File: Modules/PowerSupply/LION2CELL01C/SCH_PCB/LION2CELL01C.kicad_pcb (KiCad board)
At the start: 2 copper layers, 80.8 x 60.5 mm, 98 parts, among them J1 JUMP_4X2, J10 JUMP_2x1, J11 JUMP_2x1, J12 JUMP_2x1, J13 JUMP_4X2, J14 JUMP_2x1, J2 JUMP_2x1, J3 JUMP_2x1, J4 JUMP_2x1, J5 JUMP_2x1, J6 JUMP_2x1, J7 JUMP_4X2, J8 CONN1_1, J9 CONN1_1, P1 _, P2 _, P3 _, P4 _, Q1 IRLML6244, Q2 MMBF170LT1G, Q3 MMBF170LT1G, Q4 BSS83P, SW1 SW_PUSH, U1 BQ29209, U2 BQ24103, U3 BQ34Z100, U4 SN74HC164D

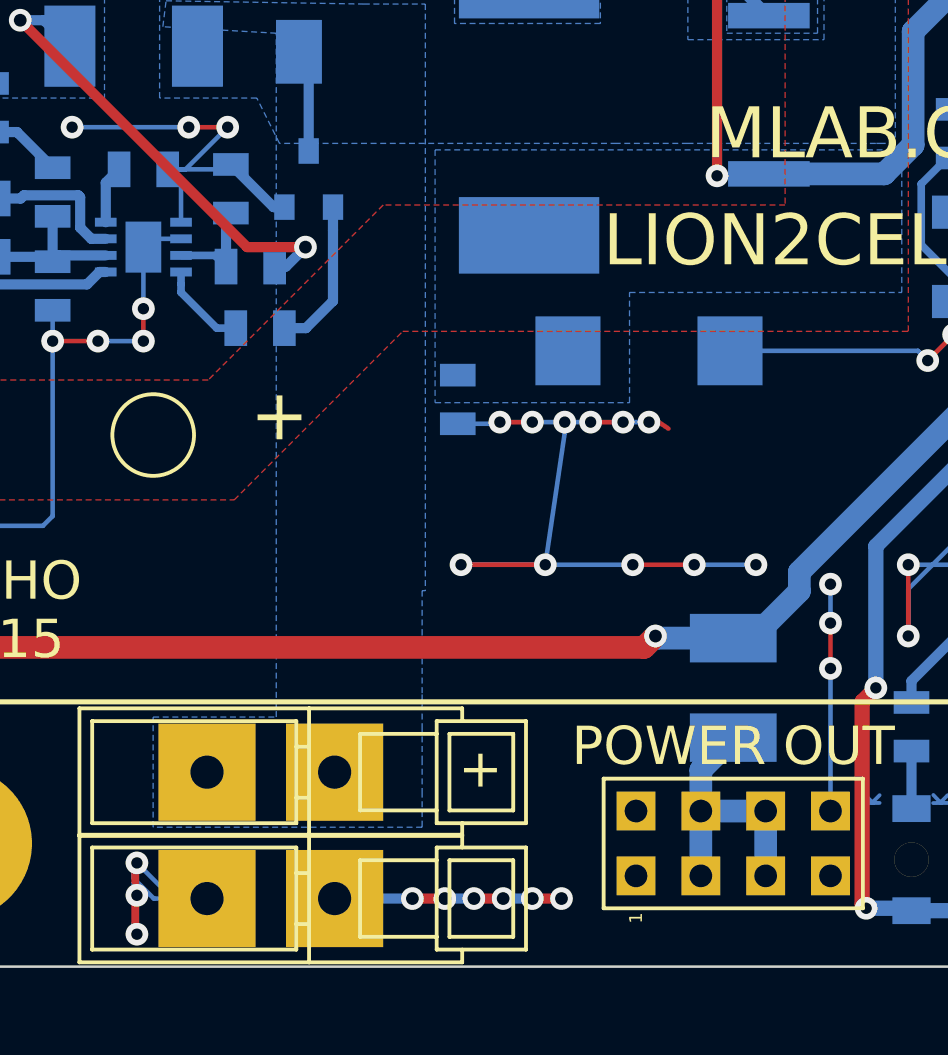
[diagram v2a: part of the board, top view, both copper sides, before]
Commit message: 
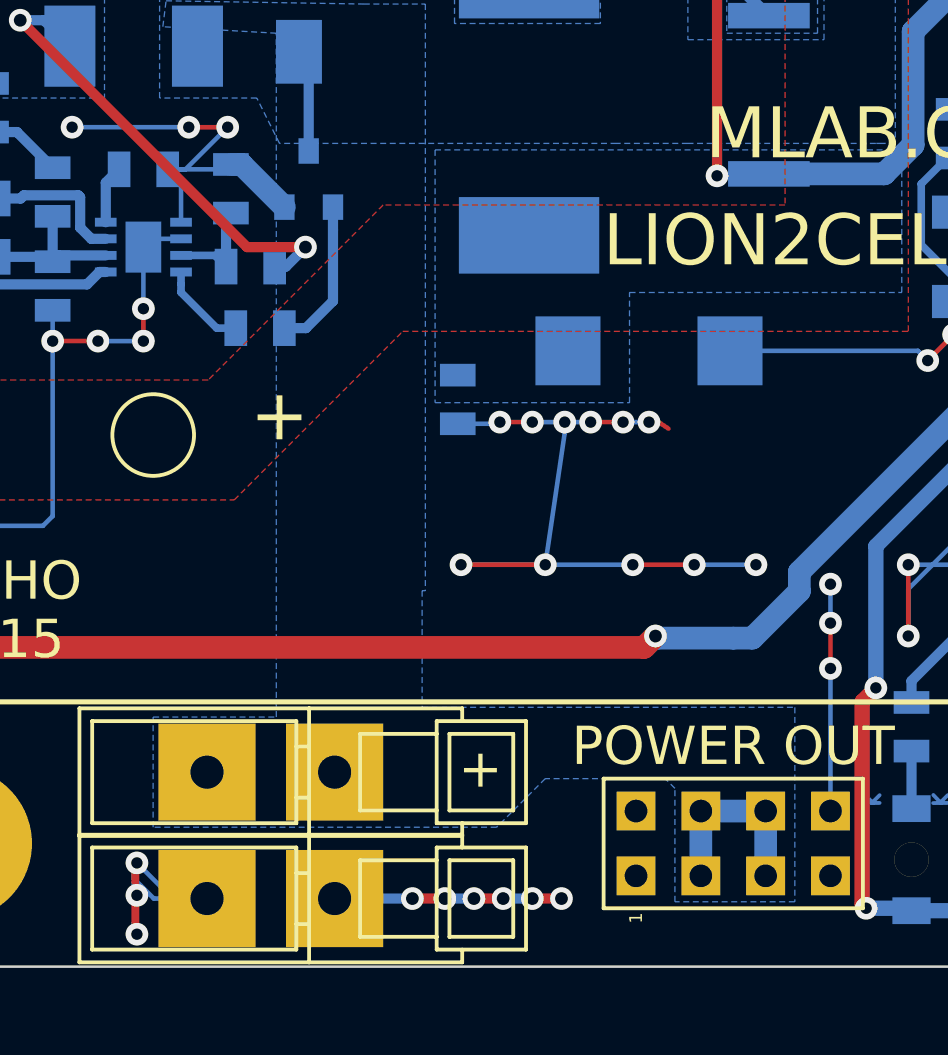
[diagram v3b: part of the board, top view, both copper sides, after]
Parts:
- removed F2: 1,1A, Mlab_F:1812
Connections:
- J7 pad 3: Net-(F2-Pad1) -> /BATTERY+
- J7 pad 4: Net-(F2-Pad1) -> /BATTERY+
- J7 pad 5: Net-(F2-Pad1) -> /BATTERY+
- J7 pad 6: Net-(F2-Pad1) -> /BATTERY+
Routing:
- net Net-(F2-Pad1): track 11.0 -> 0.00 mm
- net /BATTERY+: track 4.04 -> 11.7 mm
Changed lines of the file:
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@@
-(kicad_pcb (version 4) (host pcbnew "(2015-05-13 BZR 5653)-product")
+(kicad_pcb (version 4) (host pcbnew 4.0.0-rc1-stable)
   (general
-    (links 210)
+    (links 209)
     (no_connects 0)
     (area 0.203999 -60.756001 81.076001 -0.203999)
     (thickness 1.6)
     (drawings 31)
-    (tracks 821)
+    (tracks 819)
     (zones 0)
-    (modules 98)
-    (nets 64)
+    (modules 97)
+    (nets 63)
   )
   (page A4)
@@
   )
   (setup
-    (last_trace_width 0.18)
+    (last_trace_width 0.89)
     (user_trace_width 0.2)
     (user_trace_width 0.25)
@@
   (net 60 "Net-(D14-Pad2)")
   (net 61 "Net-(R34-Pad2)")
-  (net 62 "Net-(F2-Pad1)")
-  (net 63 "Net-(F3-Pad1)")
+  (net 62 "Net-(F3-Pad1)")
   (net_class Default "Toto je výchozí třída sítě."
     (clearance 0.18)
@@
     (add_net "Net-(D8-Pad2)")
     (add_net "Net-(D9-Pad2)")
-    (add_net "Net-(F2-Pad1)")
     (add_net "Net-(F3-Pad1)")
     (add_net "Net-(L1-Pad1)")
@@
       (net 3 GND))
     (pad 3 thru_hole rect (at -1.27 -1.27 90) (size 1.524 1.524) (drill 0.889) (layers *.Cu *.Mask F.SilkS)
-      (net 62 "Net-(F2-Pad1)"))
+      (net 56 /BATTERY+))
     (pad 4 thru_hole rect (at 1.27 -1.27 90) (size 1.524 1.524) (drill 0.889) (layers *.Cu *.Mask F.SilkS)
-      (net 62 "Net-(F2-Pad1)"))
+      (net 56 /BATTERY+))
     (pad 5 thru_hole rect (at -1.27 1.27 90) (size 1.524 1.524) (drill 0.889) (layers *.Cu *.Mask F.SilkS)
-      (net 62 "Net-(F2-Pad1)"))
+      (net 56 /BATTERY+))
     (pad 6 thru_hole rect (at 1.27 1.27 90) (size 1.524 1.524) (drill 0.889) (layers *.Cu *.Mask F.SilkS)
-      (net 62 "Net-(F2-Pad1)"))
+      (net 56 /BATTERY+))
     (pad 7 thru_hole rect (at -1.27 3.81 90) (size 1.524 1.524) (drill 0.889) (layers *.Cu *.Mask F.SilkS)
       (net 3 GND))
@@
     (fp_line (start -2.6 1.825) (end 2.6 1.825) (layer B.SilkS) (width 0.15))
     (pad 1 smd rect (at -3.1 0 270) (size 1 3.2) (layers B.Cu B.Paste B.Mask)
-      (net 63 "Net-(F3-Pad1)"))
+      (net 62 "Net-(F3-Pad1)"))
     (pad 2 smd rect (at 3.1 0 270) (size 1 3.2) (layers B.Cu B.Paste B.Mask)
       (net 10 "Net-(C10-Pad1)"))
@@
       (net 31 /CELLS))
     (pad 14 smd rect (at 0.75 1.725 90) (size 0.28 0.85) (layers B.Cu B.Paste B.Mask)
-      (net 63 "Net-(F3-Pad1)"))
+      (net 62 "Net-(F3-Pad1)"))
     (pad 15 smd rect (at 0.25 1.725 90) (size 0.28 0.85) (layers B.Cu B.Paste B.Mask)
       (net 10 "Net-(C10-Pad1)"))
@@
     )
   )
-  (module Mlab_F:1812 (layer B.Cu)
-    (at 35.56 -11.176 90)
-    (descr "Diode Mini-MELF Standard")
-    (tags "Diode Mini-MELF Standard")
-    (attr smd)
-    (fp_text reference F2 (at 0.13462 3.15468 90) (layer B.SilkS)
-      (effects (font (thickness 0.3048)) (justify mirror))
-    )
-    (fp_text value 1,1A (at 0 -3.81 90) (layer B.SilkS) hide
-      (effects (font (thickness 0.3048)) (justify mirror))
-    )
-    (fp_line (start -1.143 -1.778) (end 1.143 -1.778) (layer B.SilkS) (width 0.15))
-    (fp_line (start -1.143 1.778) (end 1.143 1.778) (layer B.SilkS) (width 0.15))
-    (pad 1 smd rect (at -1.95 0 90) (size 1.9 3.4) (layers B.Cu B.Paste B.Mask)
-      (net 62 "Net-(F2-Pad1)"))
-    (pad 2 smd rect (at 1.95 0 90) (size 1.9 3.4) (layers B.Cu B.Paste B.Mask)
-      (net 1 /BAT+))
-    (model MLAB_3D/Diodes/MiniMELF_DO213AA.wrl
-      (at (xyz 0 0 0))
-      (scale (xyz 0.3937 0.3937 0.3937))
-      (rotate (xyz 0 0 0))
-    )
-  )
   (module Mlab_F:2410 (layer B.Cu)
     (at 40.386 -40.894)
@@
     (fp_line (start -1.143 1.778) (end 1.143 1.778) (layer B.SilkS) (width 0.15))
     (pad 1 smd rect (at -2.5 0) (size 2 3.18) (layers B.Cu B.Paste B.Mask)
-      (net 63 "Net-(F3-Pad1)"))
+      (net 62 "Net-(F3-Pad1)"))
     (pad 2 smd rect (at 2.5 0) (size 2 3.18) (layers B.Cu B.Paste B.Mask)
       (net 56 /BATTERY+))
@@
   (segment (start 6.7945 -28.067) (end 8.6995 -28.067) (width 0.4) (layer B.Cu) (net 2))
   (segment (start 8.89 -27.8765) (end 8.89 -29.6545) (width 0.4) (layer B.Cu) (net 2))
+  (segment (start 17.9705 -30.01518) (end 16.29918 -31.6865) (width 0.89) (layer B.Cu) (net 3))
+  (segment (start 16.29918 -31.6865) (end 15.875 -31.6865) (width 0.89) (layer B.Cu) (net 3))
   (segment (start 59.719 -26.842) (end 59.719 -27.247) (width 0.18) (layer B.Cu) (net 3))
   (segment (start 79.502 -36.068) (end 79.502 -28.194) (width 0.18) (layer B.Cu) (net 3))
@@
   (segment (start 72.39 -17.526) (end 73.406 -16.51) (width 0.4) (layer F.Cu) (net 3))
   (segment (start 72.136 -17.526) (end 72.39 -17.526) (width 0.4) (layer F.Cu) (net 3))
-  (segment (start 17.54632 -30.01518) (end 15.875 -31.6865) (width 0.4) (layer B.Cu) (net 3))
-  (segment (start 17.9705 -30.01518) (end 17.54632 -30.01518) (width 0.4) (layer B.Cu) (net 3))
   (segment (start 43.942 -31.9405) (end 42.926 -30.9245) (width 0.3) (layer B.Cu) (net 3))
   (segment (start 44.196 -31.9405) (end 43.942 -31.9405) (width 0.3) (layer B.Cu) (net 3))
@@
   (segment (start 18.923 -32.21482) (end 18.923 -35.72002) (width 0.4) (layer B.Cu) (net 56))
   (segment (start 18.923 -35.72002) (end 18.542 -36.10102) (width 0.4) (layer B.Cu) (net 56))
+  (segment (start 34.29 -3.81) (end 34.29 -6.35) (width 0.89) (layer B.Cu) (net 56))
+  (segment (start 36.83 -6.35) (end 36.83 -3.81) (width 0.89) (layer B.Cu) (net 56))
+  (segment (start 34.29 -6.35) (end 36.83 -6.35) (width 0.89) (layer B.Cu) (net 56))
   (segment (start 62.865 -53.194) (end 62.865 -54.356) (width 0.4) (layer B.Cu) (net 57))
   (segment (start 58.394482 -22.942) (end 57.453979 -23.882503) (width 0.4) (layer B.Cu) (net 57))
@@
   (segment (start 58.439 -14.224) (end 61.214 -11.449) (width 0.4) (layer B.Cu) (net 61))
   (segment (start 61.214 -11.449) (end 61.214 -10.6045) (width 0.4) (layer B.Cu) (net 61))
-  (segment (start 34.29 -3.81) (end 34.29 -6.35) (width 0.89) (layer B.Cu) (net 62))
-  (segment (start 36.83 -6.35) (end 36.83 -3.81) (width 0.89) (layer B.Cu) (net 62))
-  (segment (start 34.29 -6.35) (end 36.83 -6.35) (width 0.89) (layer B.Cu) (net 62))
-  (segment (start 34.29 -7.956) (end 35.56 -9.226) (width 0.89) (layer B.Cu) (net 62))
-  (segment (start 34.29 -6.35) (end 34.29 -7.956) (width 0.89) (layer B.Cu) (net 62))
-  (segment (start 36.058546 -38.608) (end 36.058546 -38.415454) (width 0.4) (layer B.Cu) (net 63))
-  (segment (start 36.058546 -38.415454) (end 36.957 -37.517) (width 0.4) (layer B.Cu) (net 63))
-  (segment (start 36.058546 -38.344546) (end 36.886092 -37.517) (width 0.4) (layer B.Cu) (net 63))
-  (segment (start 36.886092 -37.517) (end 36.957 -37.517) (width 0.4) (layer B.Cu) (net 63))
-  (segment (start 36.058546 -39.315454) (end 33.254539 -42.119461) (width 0.4) (layer B.Cu) (net 63))
-  (segment (start 36.058546 -39.315454) (end 36.058546 -38.608) (width 0.4) (layer B.Cu) (net 63))
-  (segment (start 36.058546 -38.608) (end 36.058546 -38.344546) (width 0.4) (layer B.Cu) (net 63))
-  (segment (start 33.254539 -42.119461) (end 31.036 -44.338) (width 0.4) (layer B.Cu) (net 63))
-  (segment (start 29.223 -44.413) (end 29.400875 -44.413) (width 0.25) (layer B.Cu) (net 63))
-  (segment (start 29.198 -44.438) (end 29.223 -44.413) (width 0.25) (layer B.Cu) (net 63))
-  (segment (start 28.776 -44.438) (end 29.198 -44.438) (width 0.25) (layer B.Cu) (net 63))
-  (segment (start 29.400875 -44.413) (end 30.988 -44.413) (width 0.25) (layer B.Cu) (net 63))
-  (segment (start 31.036 -44.338) (end 30.988 -44.338) (width 0.4) (layer B.Cu) (net 63))
+  (segment (start 36.058546 -38.608) (end 36.058546 -38.415454) (width 0.4) (layer B.Cu) (net 62))
+  (segment (start 36.058546 -38.415454) (end 36.957 -37.517) (width 0.4) (layer B.Cu) (net 62))
+  (segment (start 36.058546 -38.344546) (end 36.886092 -37.517) (width 0.4) (layer B.Cu) (net 62))
+  (segment (start 36.886092 -37.517) (end 36.957 -37.517) (width 0.4) (layer B.Cu) (net 62))
+  (segment (start 36.058546 -39.315454) (end 33.254539 -42.119461) (width 0.4) (layer B.Cu) (net 62))
+  (segment (start 36.058546 -39.315454) (end 36.058546 -38.608) (width 0.4) (layer B.Cu) (net 62))
+  (segment (start 36.058546 -38.608) (end 36.058546 -38.344546) (width 0.4) (layer B.Cu) (net 62))
+  (segment (start 33.254539 -42.119461) (end 31.036 -44.338) (width 0.4) (layer B.Cu) (net 62))
+  (segment (start 29.223 -44.413) (end 29.400875 -44.413) (width 0.25) (layer B.Cu) (net 62))
+  (segment (start 29.198 -44.438) (end 29.223 -44.413) (width 0.25) (layer B.Cu) (net 62))
+  (segment (start 28.776 -44.438) (end 29.198 -44.438) (width 0.25) (layer B.Cu) (net 62))
+  (segment (start 29.400875 -44.413) (end 30.988 -44.413) (width 0.25) (layer B.Cu) (net 62))
+  (segment (start 31.036 -44.338) (end 30.988 -44.338) (width 0.4) (layer B.Cu) (net 62))
   (zone (net 4) (net_name "Net-(C2-Pad1)") (layer B.Cu) (hatch edge 0.508)
     (priority 1)
@@
     (polygon
       (pts
-        (xy 23.368 -10.922) (xy 23.368 -9.652) (xy 23.368 -8.382) (xy 23.368 -7.112) (xy 23.368 -6.35)
-        (xy 23.368 -5.842) (xy 23.368 -5.715) (xy 12.827 -5.715) (xy 12.827 -10.033) (xy 17.653 -10.033)
-        (xy 17.653 -36.83) (xy 13.208 -37.084) (xy 13.335 -38.1) (xy 21.082 -37.973) (xy 23.495 -37.973)
-        (xy 23.495 -14.986) (xy 23.368 -14.986) (xy 23.368 -13.462)
+        (xy 21.082 -37.973) (xy 23.495 -37.973) (xy 23.495 -14.986) (xy 23.368 -14.986) (xy 23.368 -10.414)
+        (xy 37.973 -10.414) (xy 37.973 -2.794) (xy 33.274 -2.794) (xy 33.274 -7.239) (xy 32.893 -7.62)
+        (xy 28.194 -7.62) (xy 26.289 -5.715) (xy 12.827 -5.715) (xy 12.827 -10.033) (xy 17.653 -10.033)
+        (xy 17.653 -36.83) (xy 13.208 -37.084) (xy 13.335 -38.1) (xy 21.082 -37.973)
       )
     )
@@
     )
   )
-  (zone (net 63) (net_name "Net-(F3-Pad1)") (layer B.Cu) (hatch edge 0.508)
+  (zone (net 62) (net_name "Net-(F3-Pad1)") (layer B.Cu) (hatch edge 0.508)
     (priority 1)
     (connect_pads yes (clearance 0.508))

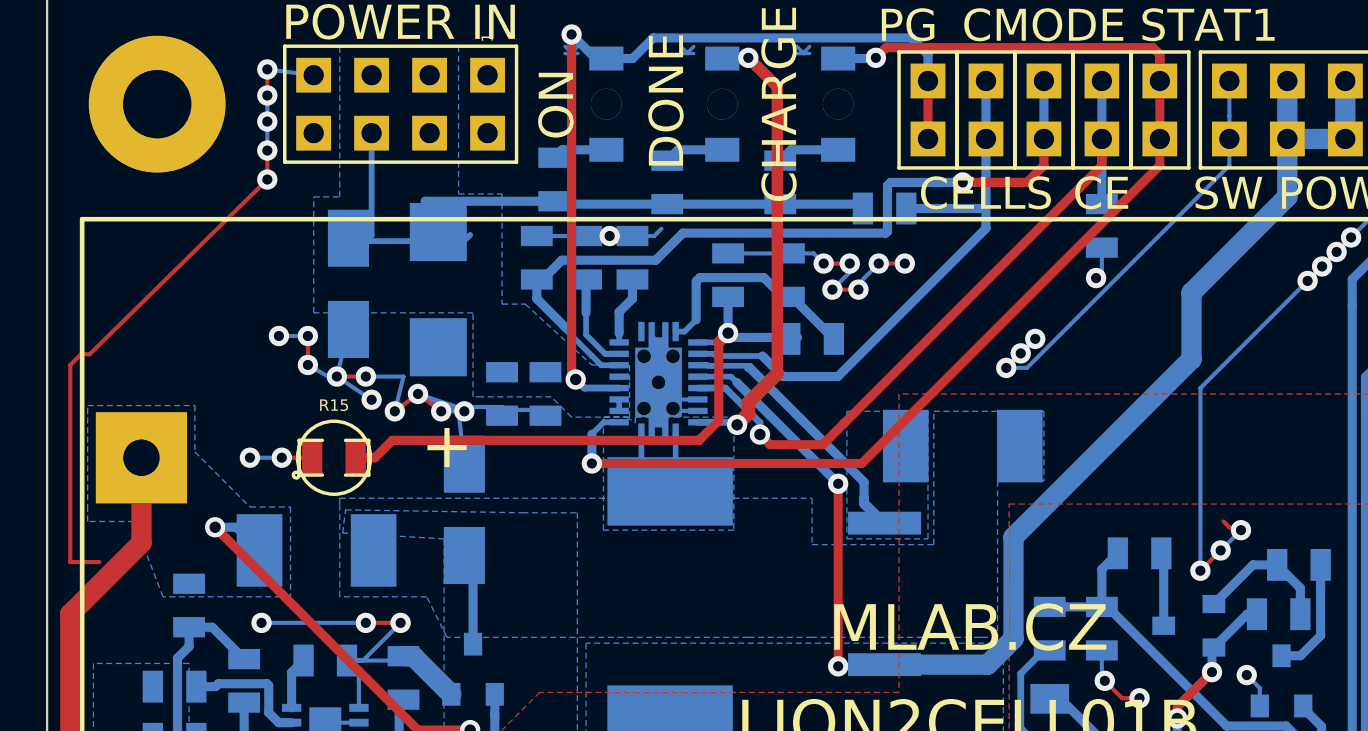
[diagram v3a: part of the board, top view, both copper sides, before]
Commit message: Uprava LION2CELL01C. Generovani vyrobnich dat.
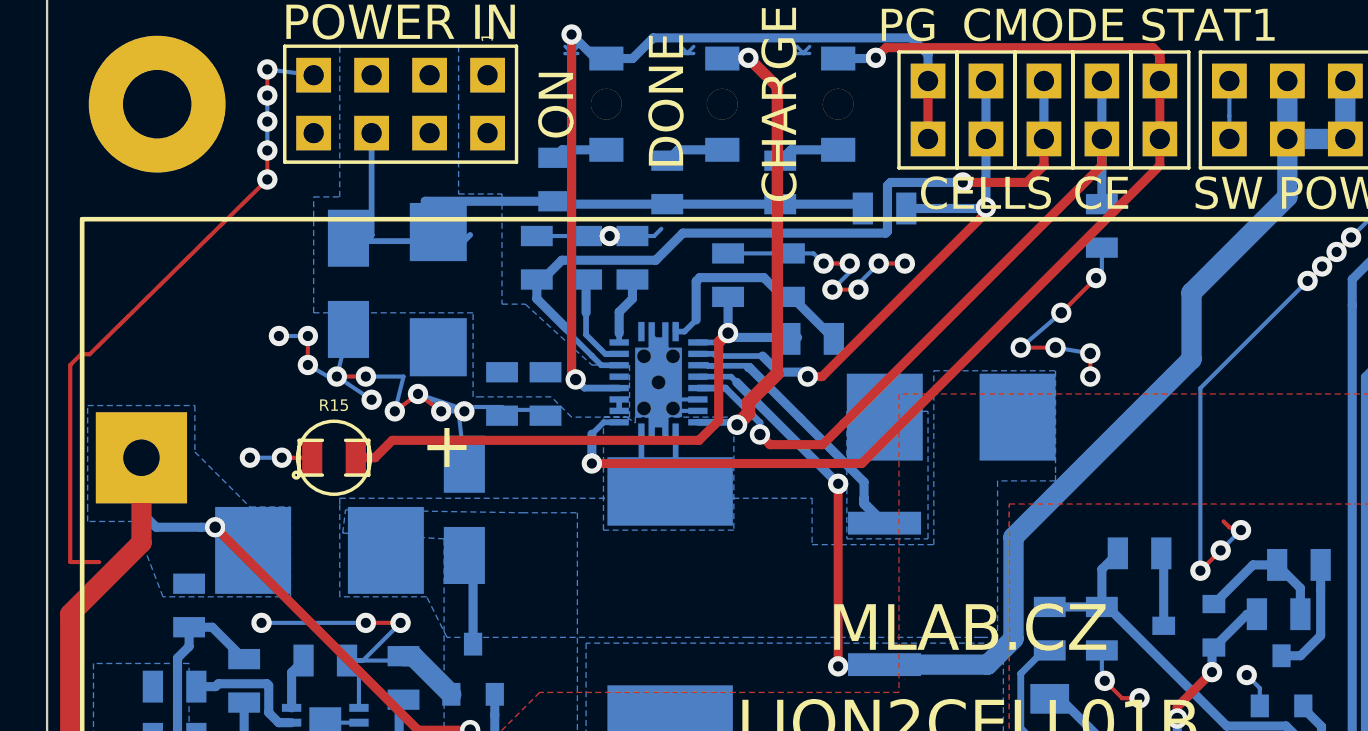
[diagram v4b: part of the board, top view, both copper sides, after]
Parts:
- BT1: value 2x18650_LION -> 2x18650_LION-RESCUE-LION2CELL01C
- F1, F3: footprint Mlab_F:2410 -> Mlab_F:Drzak_2410
- R27, R28, R29, R30, R31, R32, R33, R34: value 1K -> 2K2
- moved F3 1.37 mm to (39.9, -42.2)
- moved F1 0.13 mm to (12.2, -36.3)
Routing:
- net GND: track 414.6 -> 406.8 mm, vias 112 -> 114
- net /BAT+: track 110.0 -> 115.9 mm
- net /CELLS: track 25.7 -> 25.3 mm, vias 0 -> 2
